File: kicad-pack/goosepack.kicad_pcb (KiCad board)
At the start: 4 copper layers, 72 parts, among them J1 USB_C_Receptacle_USB2.0_16P, J11 Balance, J2 Pack lead, J3 XT30UPB-M, Q2 IRF8736, Q3 IRF8736, U13 BQ7791501, U7 BQ25798

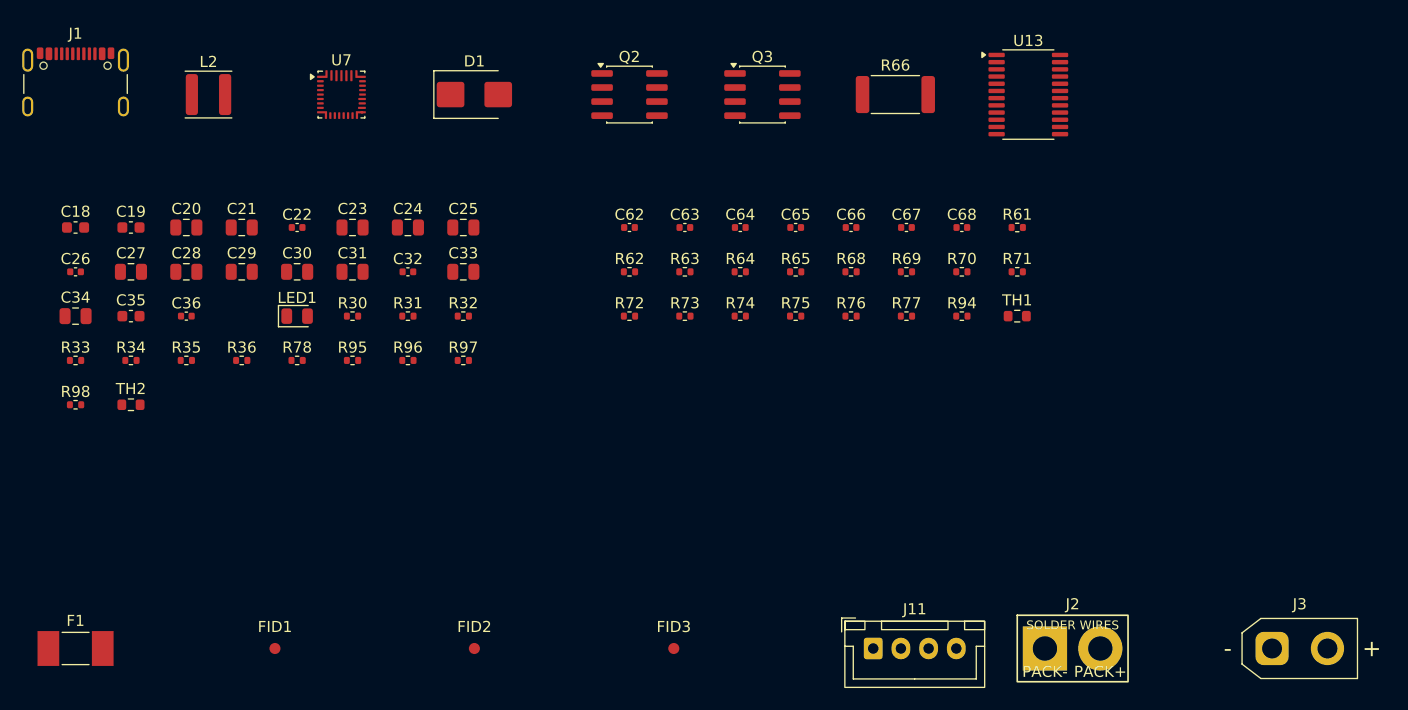
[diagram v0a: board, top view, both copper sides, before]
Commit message: Rework the pack charger layout and route the pack board with grid_router
The 3S pack board (kicad-pack/goosepack, 50 x 23 mm, 4 layers) is placed,
routed and finished by scripts alone: tools/place_pack.py compact, then
tools/route_pack.py setup / route / finish, then tools/silk.py pack.

Placement and setup:
- Charger power stage after TI's BQ25798 layout example: U7's power pins
  face L2, SYS and PMID cap rows on F.Cu pours at the pins with the 100 nF
  caps nearest, PGND out between L2's pads to vias under its body.
- Kelvin sense from R66's pad edges to R68/R69 on B.Cu, kept off the fills
  by rule areas.
- Both boot loops laid in setup: C18 under L2 on the SW1 pour, BTST1 by
  B.Cu; C19 over pin 19, SW2 back by In2.
- Setup escapes for U7's crowded corners and J1's CC2/VBUS pads, a stub out
  of C36's SDRV pad; finish drops escape vias the router didn't use.
- grid_router: per-net "router keepout" rule areas (ILIM_HIZ stays 1 mm off
  the SW2 run), via sizes by net class (signals 0.45/0.25, power 0.5/0.3 or
  0.6/0.3), no via within 0.2 mm of an SMD pad.
- ROUTE_ORDER /STAT,/CHG_SYS,/BTST1,/PROG, then the router's own order.

DRC with zones refilled: 0 errors, 0 unconnected, schematic parity clean.
A fresh-eyes review scored the layout 3.5/5 with no blockers.

Parts: C18/C19 now 0402 (C192385, extended), D1 now SMBJ15A (C19077569,
24.4 V clamp under the BQ25798's 30 V VBUS maximum). The pack is ordered
with ENIG. Silk gets polarity labels at both pigtails and the balance pins.

Also adds the route_loop.py / route_llm.py / escape.py diagnose-and-retry
tools that found the route order.

Co-Authored-By: Claude Opus 5.5 <noreply@anthropic.com>
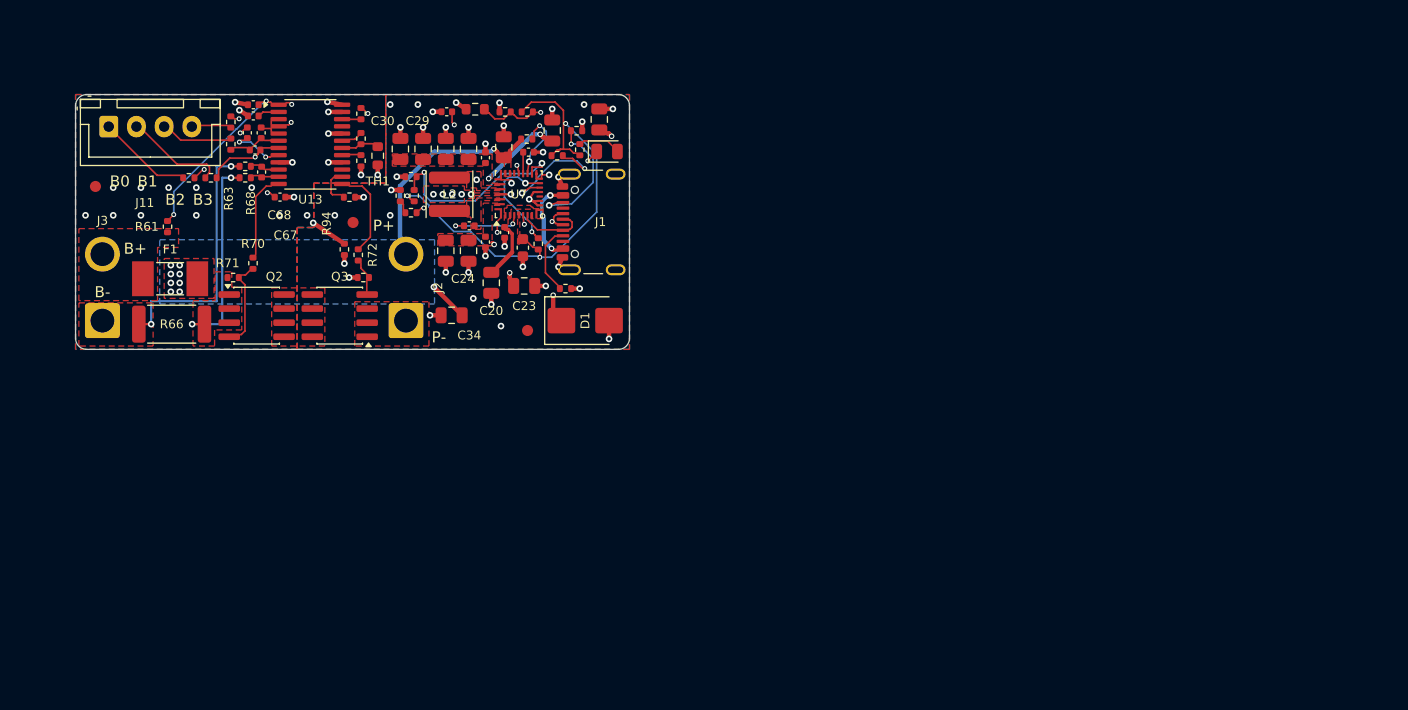
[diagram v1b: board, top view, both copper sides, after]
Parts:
- C18, C19: footprint Capacitor_SMD:C_0603_1608Metric -> Capacitor_SMD:C_0402_1005Metric
- D1: value SMBJ20A -> SMBJ15A
- J2: footprint hexy:XT30_SolderPads_1x02_P5.00mm -> Connector_Wire:SolderWire-1.5sqmm_1x02_P6mm_D1.7mm_OD3mm
- J3: value XT30UPB-M -> Cell pigtail; footprint hexy:AMASS_XT30UPB-M_1x02_P5.0mm_Vertical_EasyEDA3D -> Connector_Wire:SolderWire-1.5sqmm_1x02_P6mm_D1.7mm_OD3mm
- R79: renamed from TH2; value 10k B3434 -> 10k
- moved J3 109.6 mm to (102.4, 120.4), turned to 90 degrees
- moved J11 83.5 mm to (103.0, 102.9)
- moved R61 76.7 mm to (108.3, 111.9), turned to 90 degrees
- moved R71 70.8 mm to (114.2, 116.5), turned to 180 degrees
- moved R66 68.5 mm to (108.7, 120.7)
- moved J2 67.1 mm to (129.8, 120.4), turned to 90 degrees
- moved U13 65.0 mm to (121.2, 104.5)
- moved R70 64.0 mm to (116.0, 115.2), turned to -90 degrees
- moved C68 63.4 mm to (116.8, 107.0), turned to -90 degrees
- moved R69 60.3 mm to (115.3, 107.5)
- moved TH1 59.5 mm to (127.3, 105.5), turned to -90 degrees
- moved C67 56.6 mm to (118.5, 109.3)
- moved R94 56.1 mm to (124.3, 114.0), turned to 90 degrees
- moved R68 55.5 mm to (115.3, 106.5)
- moved C66 53.9 mm to (116.8, 103.5), turned to -90 degrees
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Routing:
- net /REGN: track 0.00 -> 41.7 mm, vias 0 -> 3
- net /BAT_N: track 0.00 -> 36.8 mm, vias 0 -> 24
- net /PACK-: track 0.00 -> 31.0 mm, vias 0 -> 43
- net /VBUS: track 0.00 -> 26.4 mm, vias 0 -> 5
- net /PROT_VDD: track 0.00 -> 23.8 mm, vias 0 -> 4
- net /PACK+: track 0.00 -> 19.9 mm, vias 0 -> 10
- net /TS: track 0.00 -> 19.3 mm, vias 0 -> 2
- net /PROT_SNS: track 0.00 -> 17.8 mm, vias 0 -> 2
- net /ILIM_HIZ: track 0.00 -> 17.0 mm, vias 0 -> 2
- net /SDRV: track 0.00 -> 16.5 mm, vias 0 -> 2
- net /STAT: track 0.00 -> 13.9 mm, vias 0 -> 2
- net /PROT_VC0: track 0.00 -> 12.2 mm, vias 0 -> 4
- net /CC2: track 0.00 -> 11.2 mm, vias 0 -> 2
- net /PROG: track 0.00 -> 10.9 mm, vias 0 -> 2
- net /CHG_SCL: track 0.00 -> 10.9 mm, vias 0 -> 2
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- added copper zone on B.Cu, net /BAT_N
- added copper zone on F.Cu, net /BAT_N
- added copper zone on In1.Cu, net /BAT_N
- added copper zone on In2.Cu, net /BAT_N
- added copper zone on F.Cu, net /CELL+
- added copper zone on F.Cu, net /CHG_SYS
- added copper zone on B.Cu, net /PACK+
- added copper zone on F.Cu, net /PACK+
- added copper zone on In2.Cu, net /PACK+
- added copper zone on B.Cu, net /PACK-
- added copper zone on F.Cu, net /PACK-
- added copper zone on In1.Cu, net /PACK-
- added copper zone on In2.Cu, net /PACK-
- added copper zone on F.Cu, net /PMID
- added copper zone on F.Cu, net /PROT_FET_D
- added copper zone on F.Cu, net /PROT_SNS
- added copper zone on F.Cu, net /REGN
- added copper zone on F.Cu, net /SW1
- added copper zone on F.Cu, net /SW2
- added copper zone on F.Cu, net /VBUS
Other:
- board outline added: 50 x 23 mm
- board text added: "B+"
- board text added: "B-"
- board text added: "B0"
- board text added: "B1"
- board text added: "B2"
- board text added: "B3"
- board text added: "P+"
- board text added: "P-"

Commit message: Have JLC place every 3S pack SMD part and document the pack process
- Clear DNP on L2, Q2, Q3, R66, TH1 and F1 (schematic and board); PARTS.md
  and README updated.
- Route with 0.3 mm via drills, extend ROUTE_ORDER, stage finish; lead-free
  HASL in the stackup.
- Add docs/3s-pack-process.md, the placement-to-JLC-order recipe, linked
  from the README, and the brain/pack side-by-side render.

Co-Authored-By: Claude Opus 5.5 <noreply@anthropic.com>
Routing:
- net /TS: track 19.3 -> 11.3 mm
- net /ILIM_HIZ: track 17.0 -> 23.1 mm
- net /CHG_SCL: track 10.9 -> 6.38 mm
- net /SDRV: track 16.5 -> 12.2 mm
- net /CC2: track 11.2 -> 7.35 mm
- net /PACK+: track 19.9 -> 23.4 mm
- net /CC1: track 5.42 -> 8.10 mm
- net /USB_DP: track 4.35 -> 6.99 mm
- net /STAT: track 13.9 -> 16.2 mm
- net /CHG_SDA: track 9.43 -> 7.68 mm
- net /VBUS: track 26.4 -> 27.7 mm
- net /REGN: track 41.7 -> 40.4 mm, vias 3 -> 4
- net /PMID: track 3.89 -> 4.76 mm
- net /BAT_N: vias 24 -> 23
